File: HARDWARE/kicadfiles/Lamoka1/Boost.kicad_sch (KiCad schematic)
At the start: 52 parts, among them J1 Boostconverteroutput, Q1 CSD19531Q5A, Q2 CSD19531Q5A, Q3 CSD19531Q5A, Q4 CSD19531Q5A, Q5 BSS138, U2 LM5122QMHE/NOPB, U3 LM5122QMHE/NOPB

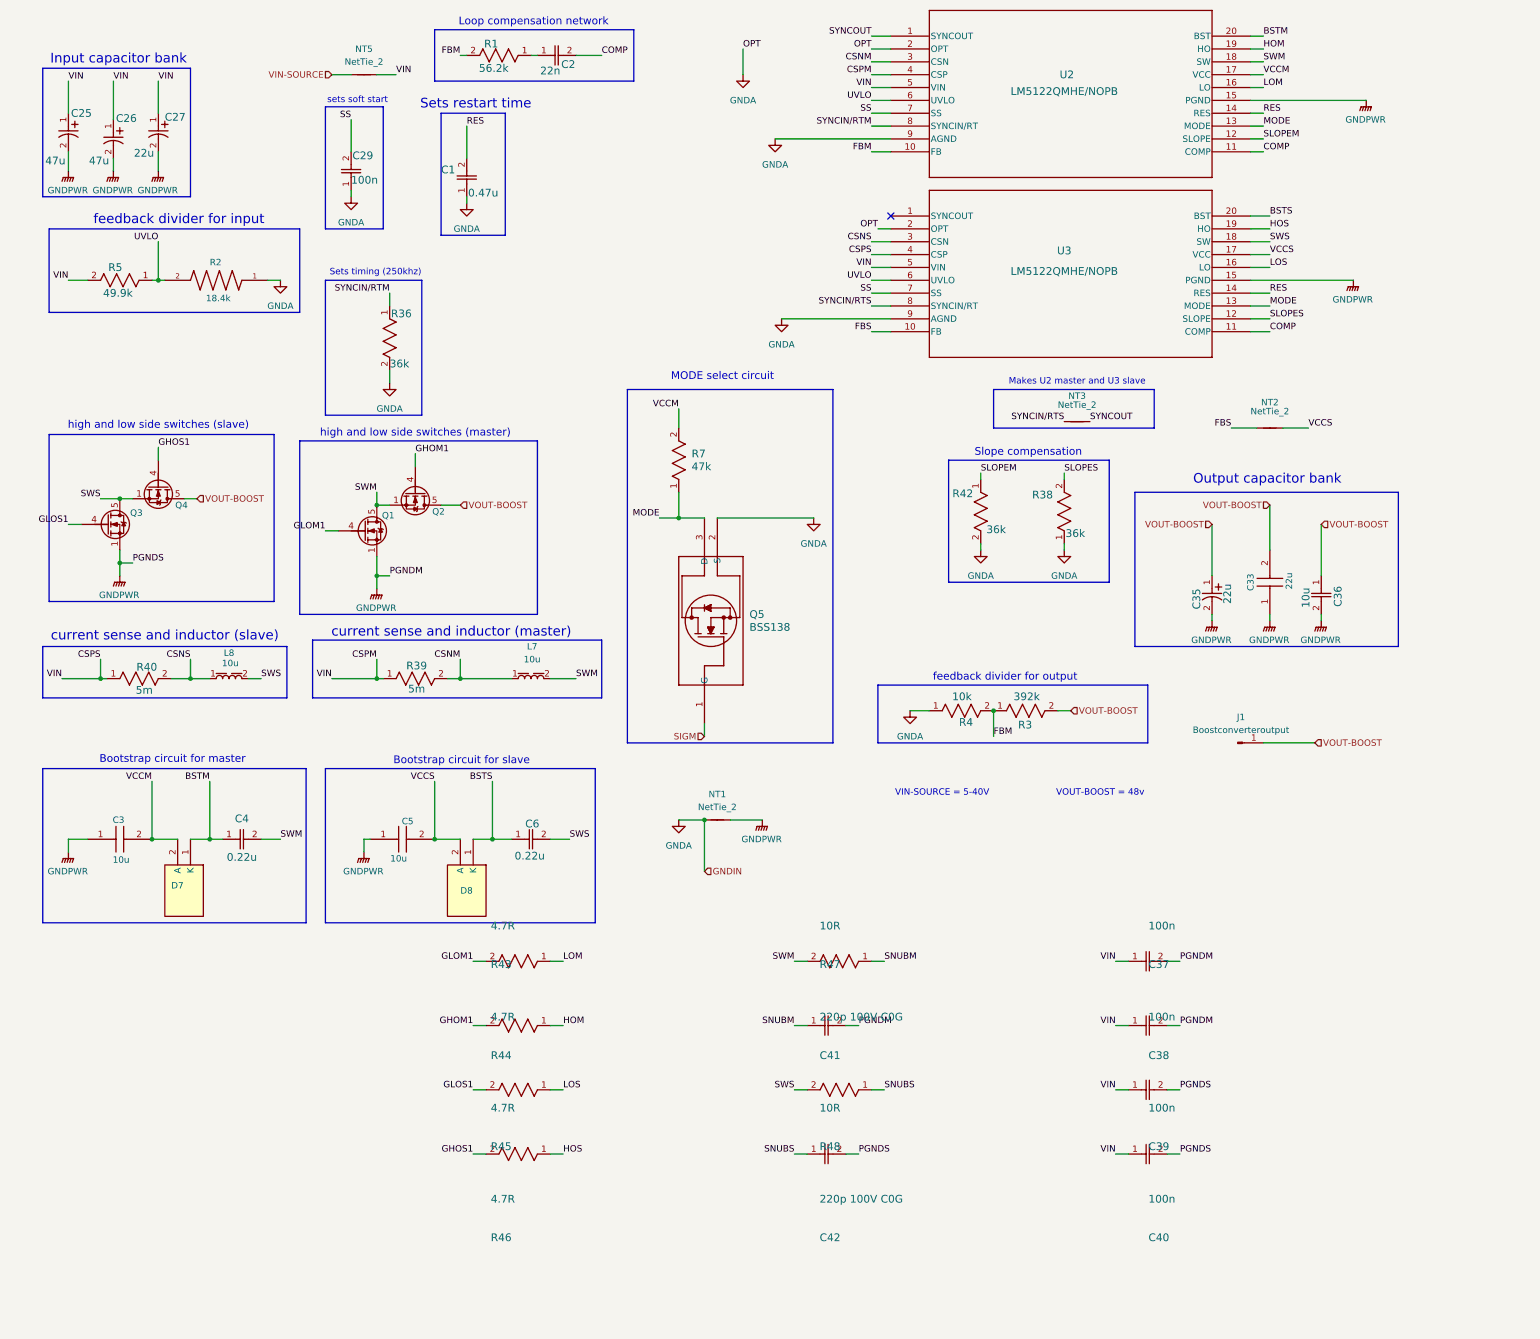
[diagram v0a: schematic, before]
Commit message: docs: Document prototype P1 schematic design improvements
Major updates to boost converter topology with LM5122 driver,
connect all section interfaces (charging, control), fix net connectivity.

This represents a near-complete functional schematic for the Lamoka1
inverter/charger system. All three main sections now have proper
interconnections for the RP2354A control implementation.
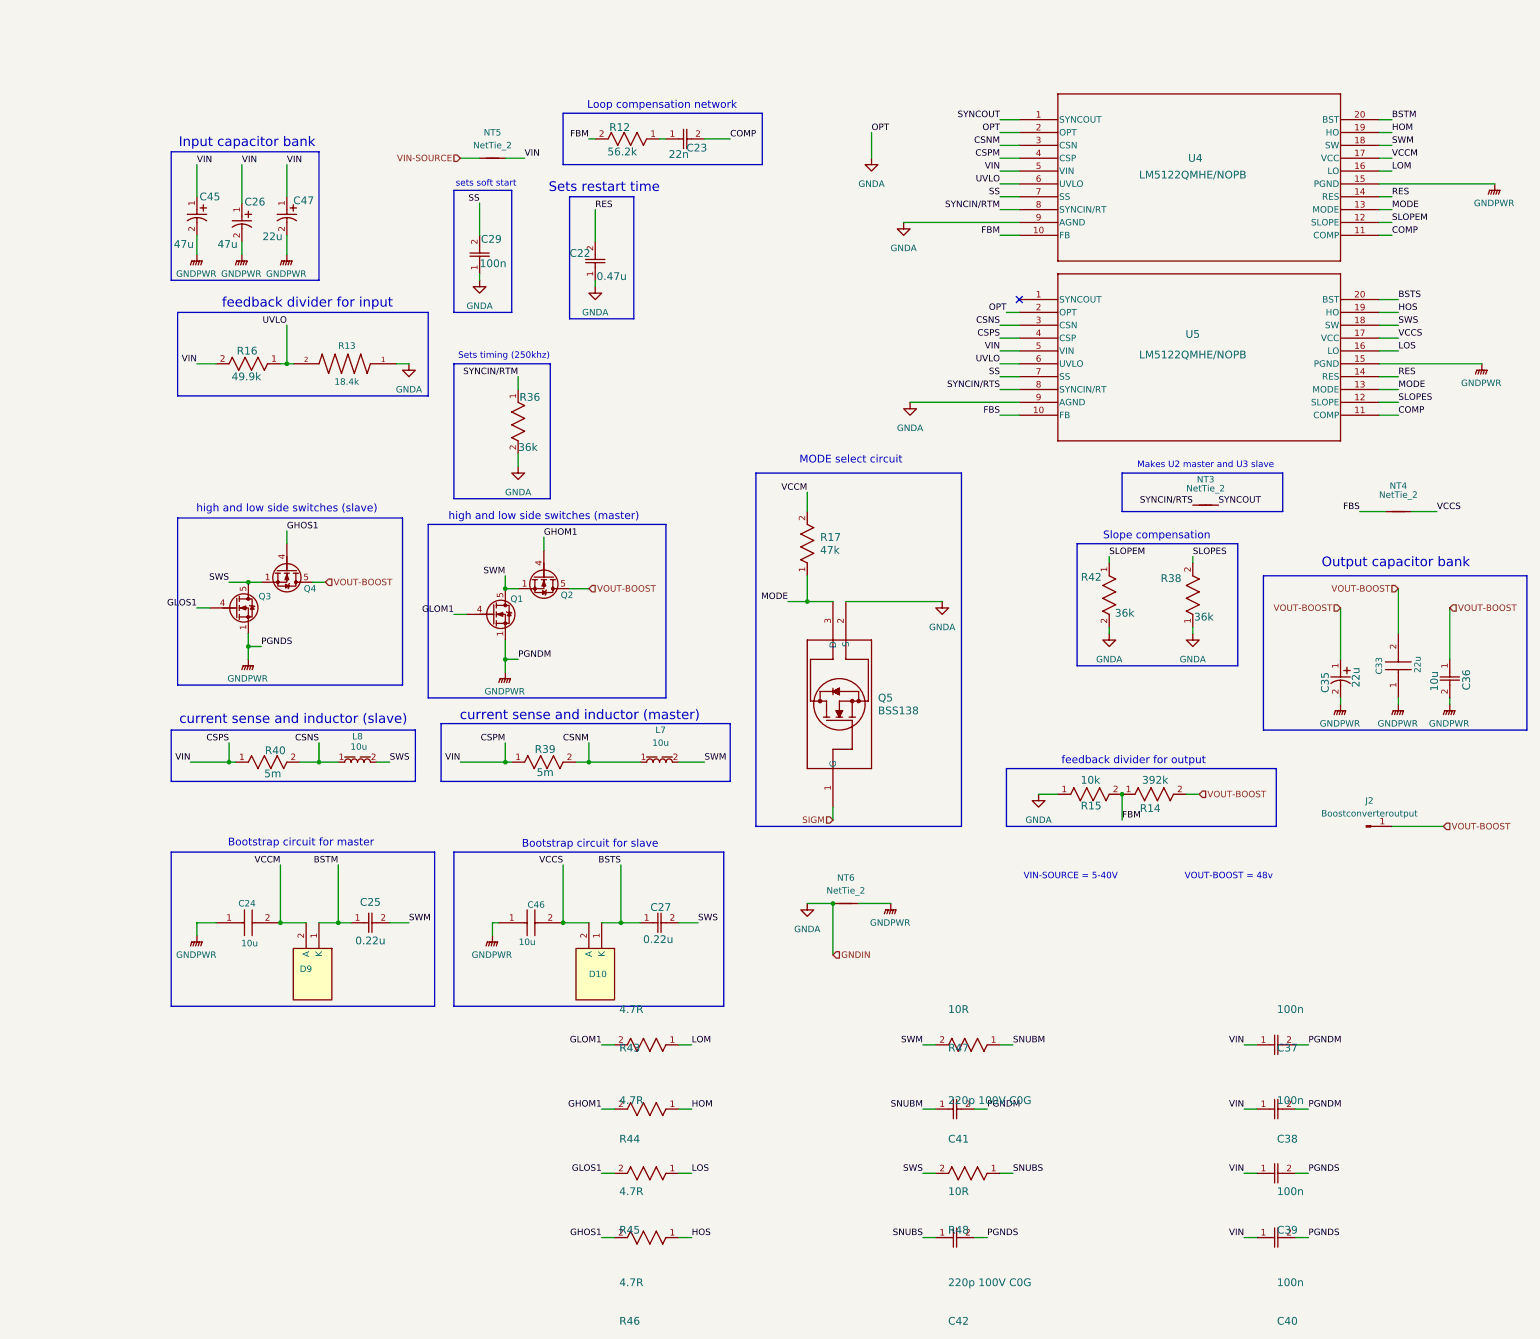
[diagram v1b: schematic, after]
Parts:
- renumbered C1 to C22, C2 to C23, C3 to C24, C4 to C25, C6 to C27, C25 to C45, C5 to C46, C27 to C47, D8 to D10, D7 to D9, J1 to J2, NT2 to NT4, NT1 to NT6, R1 to R12, R2 to R13, R3 to R14, R4 to R15, R5 to R16, R7 to R17, U2 to U4, U3 to U5
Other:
- moved on the sheet: C22, C23, C24, C25, C26, C27, C29, C33, C35, C36, C37, C38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

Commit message: Revert "docs: Document prototype P1 schematic design improvements"
This reverts commit 9a36aaba68a23f8da8ed8c8f957268abdd88419f.
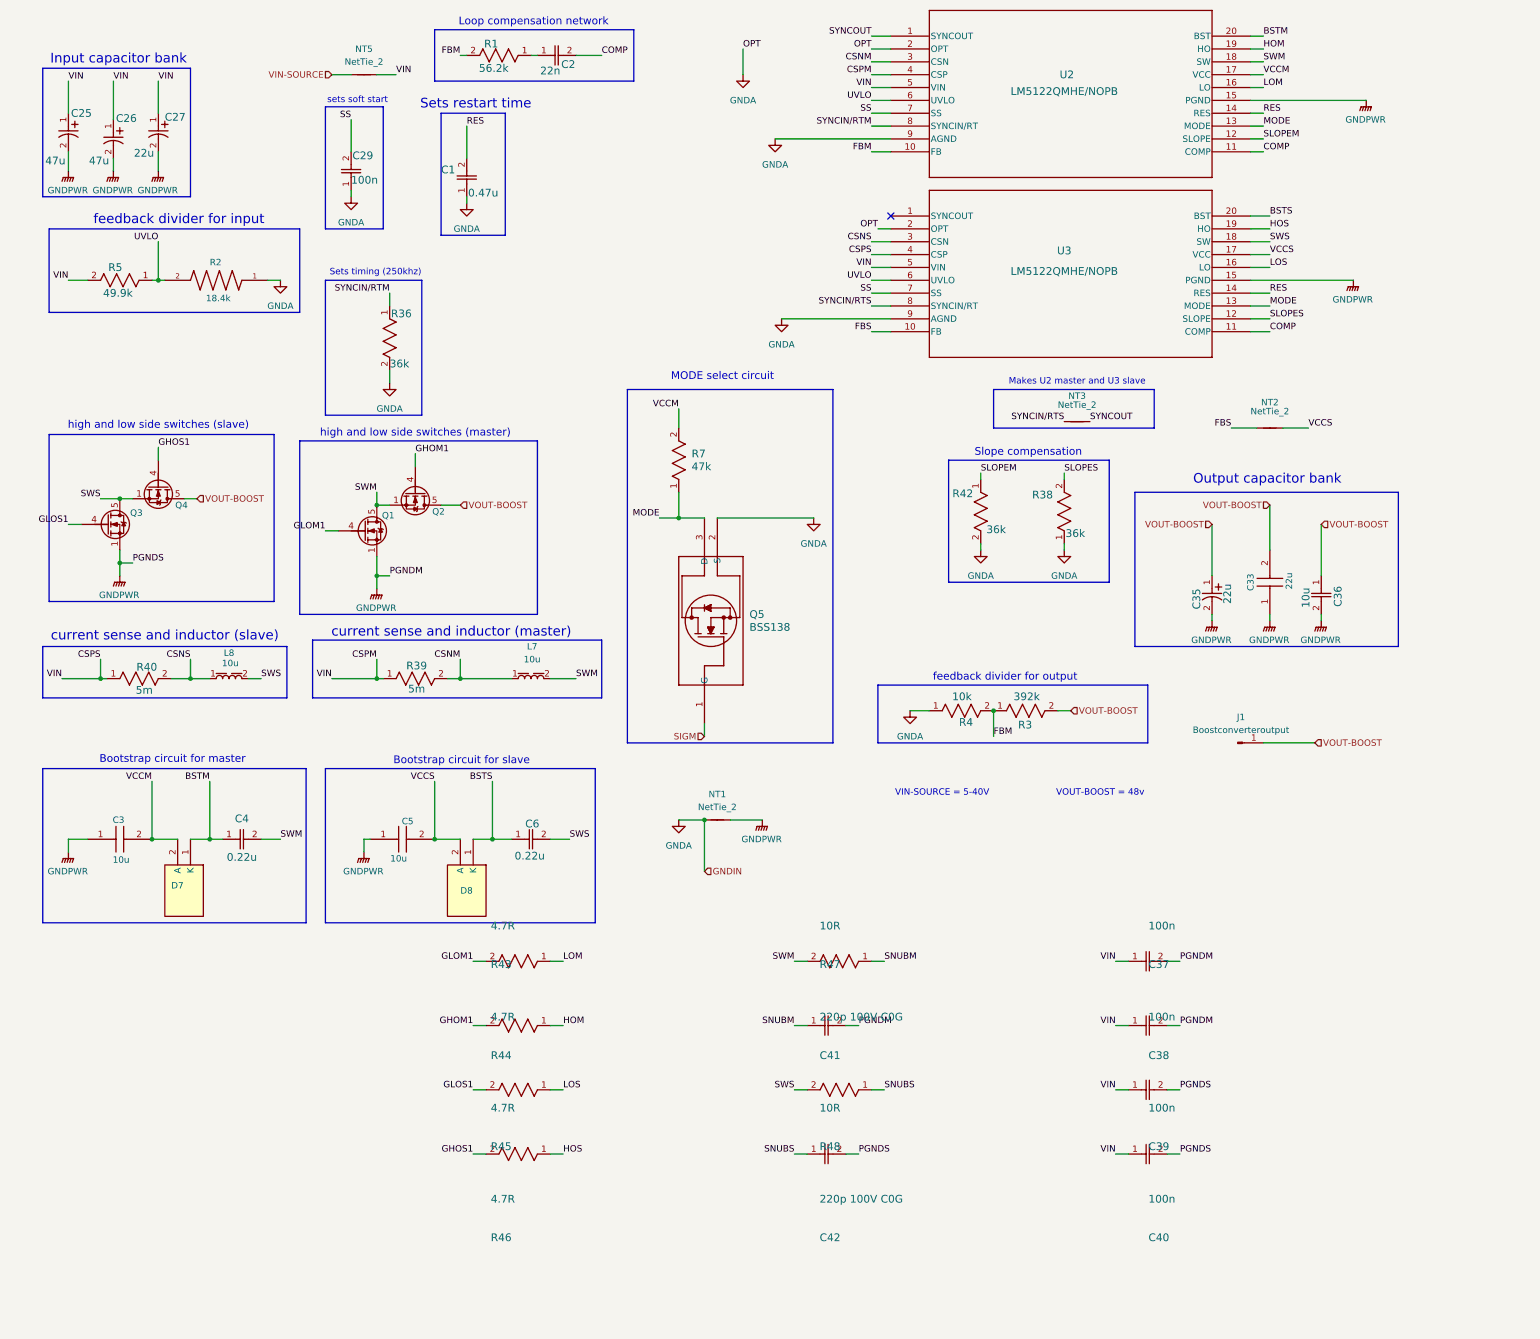
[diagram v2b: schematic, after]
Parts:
- renumbered C22 to C1, C23 to C2, C45 to C25, C47 to C27, C24 to C3, C25 to C4, C46 to C5, C27 to C6, D9 to D7, D10 to D8, J2 to J1, NT6 to NT1, NT4 to NT2, R12 to R1, R13 to R2, R14 to R3, R15 to R4, R16 to R5, R17 to R7, U4 to U2, U5 to U3
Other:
- moved on the sheet: C1, C2, C25, C26, C27, C29, C3, C33, C35, C36, C37, C38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
